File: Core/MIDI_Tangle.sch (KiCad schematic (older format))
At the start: 32 parts, among them J1 USB_C_Receptacle_USB2.0, J2 Conn_01x04, J4 Conn_01x06_Male, J5 Conn_01x08_Female, J6 Conn_01x08_Female, J7 Conn_01x08_Female, J8 Conn_01x08_Female, SW1 SW_Push_DPDT, U1 ATSAMD21G15B-A, U14 MCP2517FD-xSL, U15 TLE9250V, Y1 20MHz

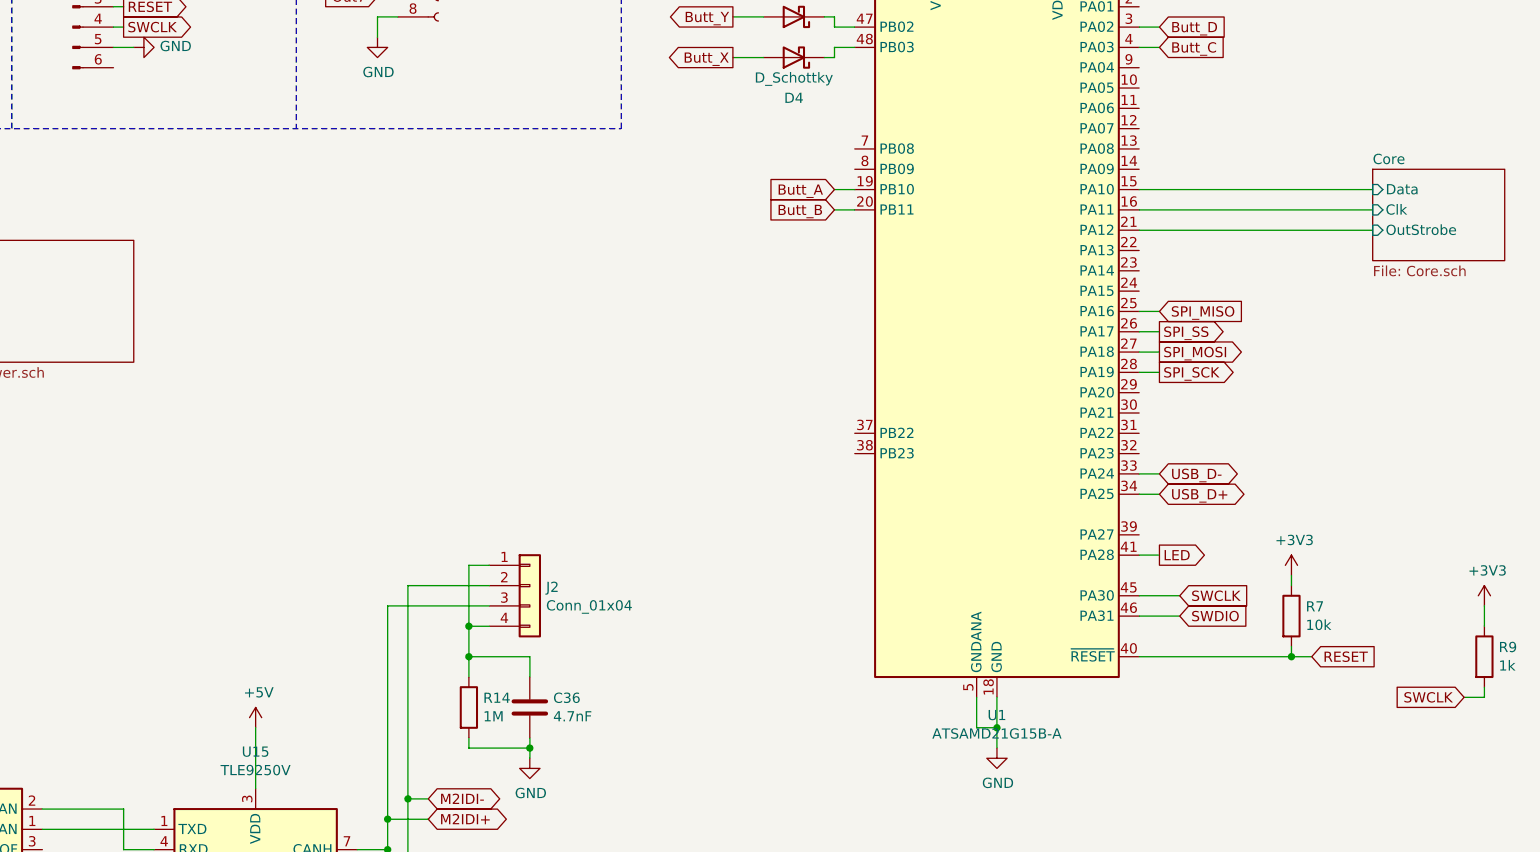
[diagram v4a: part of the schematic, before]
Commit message: Add bootloader buttons
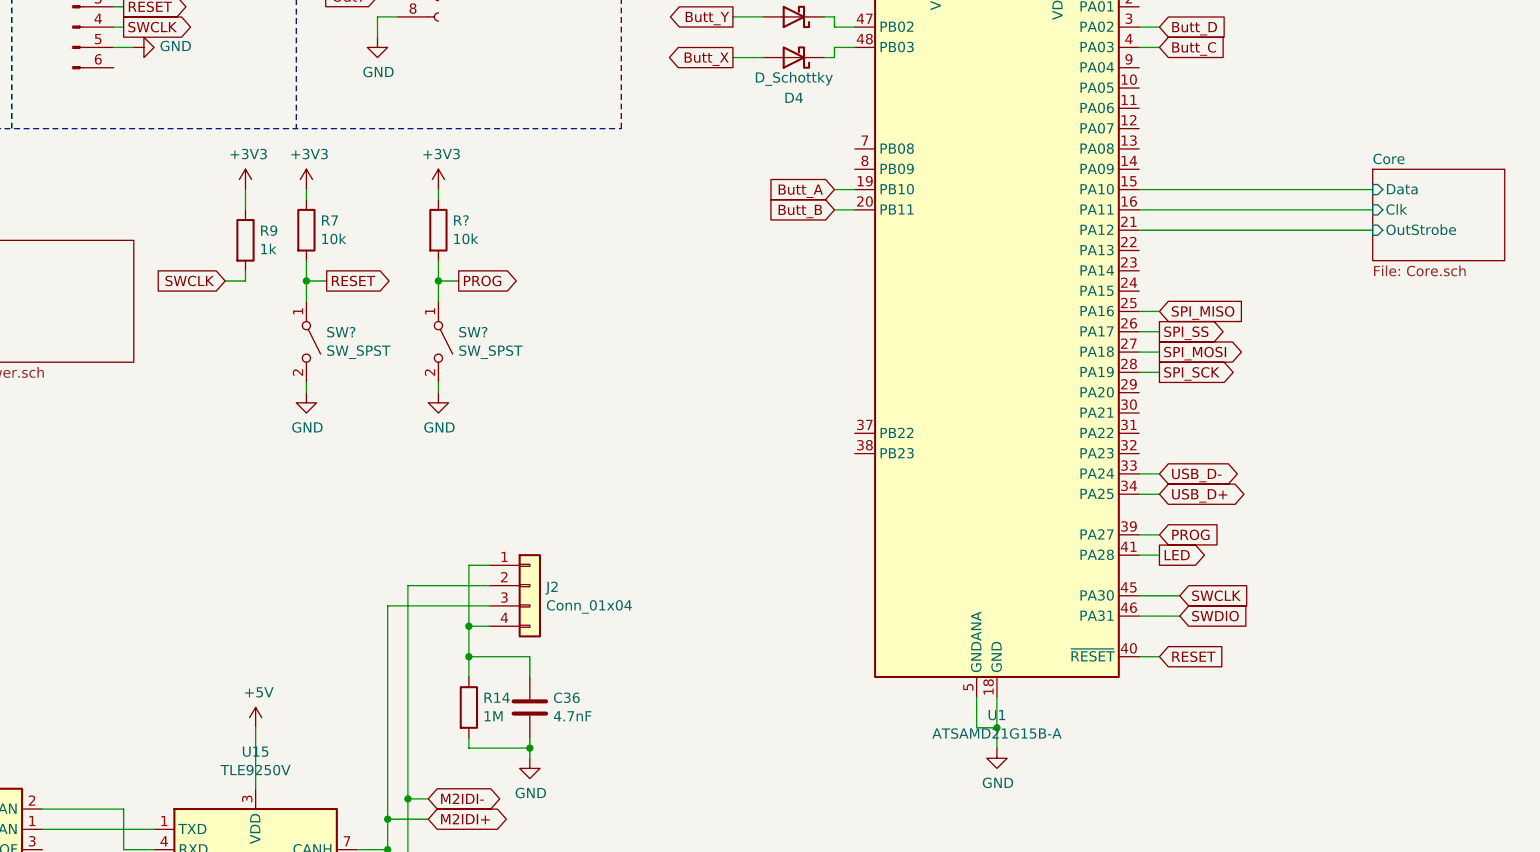
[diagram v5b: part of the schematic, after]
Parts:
- added R?: 10k, Resistor_SMD:R_0603_1608Metric, symbol Device:R
- added SW? (x2): SW_SPST, Custom_FP:Tactile_angled_5x5.4_SMD, symbol Switch:SW_SPST
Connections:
- net +3V3: now also R?.1
- net GND: now also SW?.2 (B), SW?.2 (B)
- net RESET: now also SW?.1 (A)
- net PROG: now reaches U1.39 (PA27)
- net PROG: now also R?.2, SW?.1 (A)
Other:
- moved on the sheet: R7, R9
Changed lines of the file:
@@
 Wire Wire Line
 	8450 5500 8650 5500
-Text GLabel 9300 5800 2    50   Input ~ 0
+Text GLabel 8550 5800 2    50   Input ~ 0
 RESET
 $Comp
@@
 LED
 Wire Wire Line
-	9300 5800 9200 5800
+	8550 5800 8450 5800
 $Comp
 L Device:C C3
@@
 L Device:R R7
 U 1 1 60DE3924
-P 9200 5600
-F 0 "R7" H 9270 5646 50  0000 L CNN
-F 1 "10k" H 9270 5555 50  0000 L CNN
-F 2 "Resistor_SMD:R_0603_1608Metric" V 9130 5600 50  0001 C CNN
-F 3 "~" H 9200 5600 50  0001 C CNN
-	1    9200 5600
-	1    0    0    -1
-$EndComp
-Wire Wire Line
-	9200 5750 9200 5800
-Wire Wire Line
-	9200 5800 8450 5800
+P 4350 3700
+F 0 "R7" H 4420 3746 50  0000 L CNN
+F 1 "10k" H 4420 3655 50  0000 L CNN
+F 2 "Resistor_SMD:R_0603_1608Metric" V 4280 3700 50  0001 C CNN
+F 3 "~" H 4350 3700 50  0001 C CNN
+	1    4350 3700
+	1    0    0    -1
+$EndComp
 $Comp
 L power:+3V3 #PWR0110
 U 1 1 60DF374E
-P 9200 5400
-F 0 "#PWR0110" H 9200 5250 50  0001 C CNN
-F 1 "+3V3" H 9215 5573 50  0000 C CNN
-F 2 "" H 9200 5400 50  0001 C CNN
-F 3 "" H 9200 5400 50  0001 C CNN
-	1    9200 5400
-	1    0    0    -1
-$EndComp
-Wire Wire Line
-	9200 5400 9200 5450
+P 4350 3500
+F 0 "#PWR0110" H 4350 3350 50  0001 C CNN
+F 1 "+3V3" H 4365 3673 50  0000 C CNN
+F 2 "" H 4350 3500 50  0001 C CNN
+F 3 "" H 4350 3500 50  0001 C CNN
+	1    4350 3500
+	1    0    0    -1
+$EndComp
+Wire Wire Line
+	4350 3500 4350 3550
 $Comp
 L Device:R R2
@@
 L Device:R R9
 U 1 1 60ED0663
-P 10150 5800
-F 0 "R9" H 10220 5846 50  0000 L CNN
-F 1 "1k" H 10220 5755 50  0000 L CNN
-F 2 "Resistor_SMD:R_0603_1608Metric" V 10080 5800 50  0001 C CNN
-F 3 "~" H 10150 5800 50  0001 C CNN
-	1    10150 5800
+P 4050 3750
+F 0 "R9" H 4120 3796 50  0000 L CNN
+F 1 "1k" H 4120 3705 50  0000 L CNN
+F 2 "Resistor_SMD:R_0603_1608Metric" V 3980 3750 50  0001 C CNN
+F 3 "~" H 4050 3750 50  0001 C CNN
+	1    4050 3750
 	1    0    0    -1
 $EndComp
@@
 L power:+3V3 #PWR0175
 U 1 1 60ED1510
-P 10150 5550
-F 0 "#PWR0175" H 10150 5400 50  0001 C CNN
-F 1 "+3V3" H 10165 5723 50  0000 C CNN
-F 2 "" H 10150 5550 50  0001 C CNN
-F 3 "" H 10150 5550 50  0001 C CNN
-	1    10150 5550
-	1    0    0    -1
-$EndComp
-Text GLabel 10050 6000 0    50   Input ~ 0
+P 4050 3500
+F 0 "#PWR0175" H 4050 3350 50  0001 C CNN
+F 1 "+3V3" H 4065 3673 50  0000 C CNN
+F 2 "" H 4050 3500 50  0001 C CNN
+F 3 "" H 4050 3500 50  0001 C CNN
+	1    4050 3500
+	1    0    0    -1
+$EndComp
+Text GLabel 3950 3950 0    50   Input ~ 0
 SWCLK
 Wire Wire Line
-	10050 6000 10150 6000
-Wire Wire Line
-	10150 6000 10150 5950
-Wire Wire Line
-	10150 5650 10150 5550
+	3950 3950 4050 3950
+Wire Wire Line
+	4050 3950 4050 3900
+Wire Wire Line
+	4050 3600 4050 3500
 Wire Wire Line
 	6150 1200 6250 1200
@@
 	0    1    1    0
 $EndComp
-Connection ~ 9200 5800
 $Sheet
 S 9600 3400 650  450
@@
 Wire Wire Line
 	8450 3700 9600 3700
+Text GLabel 4450 3950 2    50   Output ~ 0
+RESET
+Wire Wire Line
+	4450 3950 4350 3950
+Connection ~ 4350 3950
+Wire Wire Line
+	4350 3950 4350 4050
+Wire Wire Line
+	4350 3850 4350 3950
+$Comp
+L Switch:SW_SPST SW?
+U 1 1 65133670
+P 4350 4250
+F 0 "SW?" V 4304 4348 50  0000 L CNN
+F 1 "SW_SPST" V 4395 4348 50  0000 L CNN
+F 2 "Custom_FP:Tactile_angled_5x5.4_SMD" H 4350 4250 50  0001 C CNN
+F 3 "~" H 4350 4250 50  0001 C CNN
+	1    4350 4250
+	0    1    1    0
+$EndComp
+$Comp
+L power:GND #PWR?
+U 1 1 65133EF2
+P 4350 4500
+F 0 "#PWR?" H 4350 4250 50  0001 C CNN
+F 1 "GND" H 4355 4327 50  0000 C CNN
+F 2 "" H 4350 4500 50  0001 C CNN
+F 3 "" H 4350 4500 50  0001 C CNN
+	1    4350 4500
+	1    0    0    -1
+$EndComp
+Wire Wire Line
+	4350 4500 4350 4450
+$Comp
+L Device:R R?
+U 1 1 65140F2B
+P 5000 3700
+F 0 "R?" H 5070 3746 50  0000 L CNN
+F 1 "10k" H 5070 3655 50  0000 L CNN
+F 2 "Resistor_SMD:R_0603_1608Metric" V 4930 3700 50  0001 C CNN
+F 3 "~" H 5000 3700 50  0001 C CNN
+	1    5000 3700
+	1    0    0    -1
+$EndComp
+$Comp
+L power:+3V3 #PWR?
+U 1 1 65140F31
+P 5000 3500
+F 0 "#PWR?" H 5000 3350 50  0001 C CNN
+F 1 "+3V3" H 5015 3673 50  0000 C CNN
+F 2 "" H 5000 3500 50  0001 C CNN
+F 3 "" H 5000 3500 50  0001 C CNN
+	1    5000 3500
+	1    0    0    -1
+$EndComp
+Wire Wire Line
+	5000 3500 5000 3550
+Text GLabel 5100 3950 2    50   Output ~ 0
+PROG
+Wire Wire Line
+	5100 3950 5000 3950
+Connection ~ 5000 3950
+Wire Wire Line
+	5000 3950 5000 4050
+Wire Wire Line
+	5000 3850 5000 3950
+$Comp
+L Switch:SW_SPST SW?
+U 1 1 65140F3D
+P 5000 4250
+F 0 "SW?" V 4954 4348 50  0000 L CNN
+F 1 "SW_SPST" V 5045 4348 50  0000 L CNN
+F 2 "Custom_FP:Tactile_angled_5x5.4_SMD" H 5000 4250 50  0001 C CNN
+F 3 "~" H 5000 4250 50  0001 C CNN
+	1    5000 4250
+	0    1    1    0
+$EndComp
+$Comp
+L power:GND #PWR?
+U 1 1 65140F43
+P 5000 4500
+F 0 "#PWR?" H 5000 4250 50  0001 C CNN
+F 1 "GND" H 5005 4327 50  0000 C CNN
+F 2 "" H 5000 4500 50  0001 C CNN
+F 3 "" H 5000 4500 50  0001 C CNN
+	1    5000 4500
+	1    0    0    -1
+$EndComp
+Wire Wire Line
+	5000 4500 5000 4450
+Text GLabel 8550 5200 2    50   Input ~ 0
+PROG
+Wire Wire Line
+	8550 5200 8450 5200
 $EndSCHEMATC

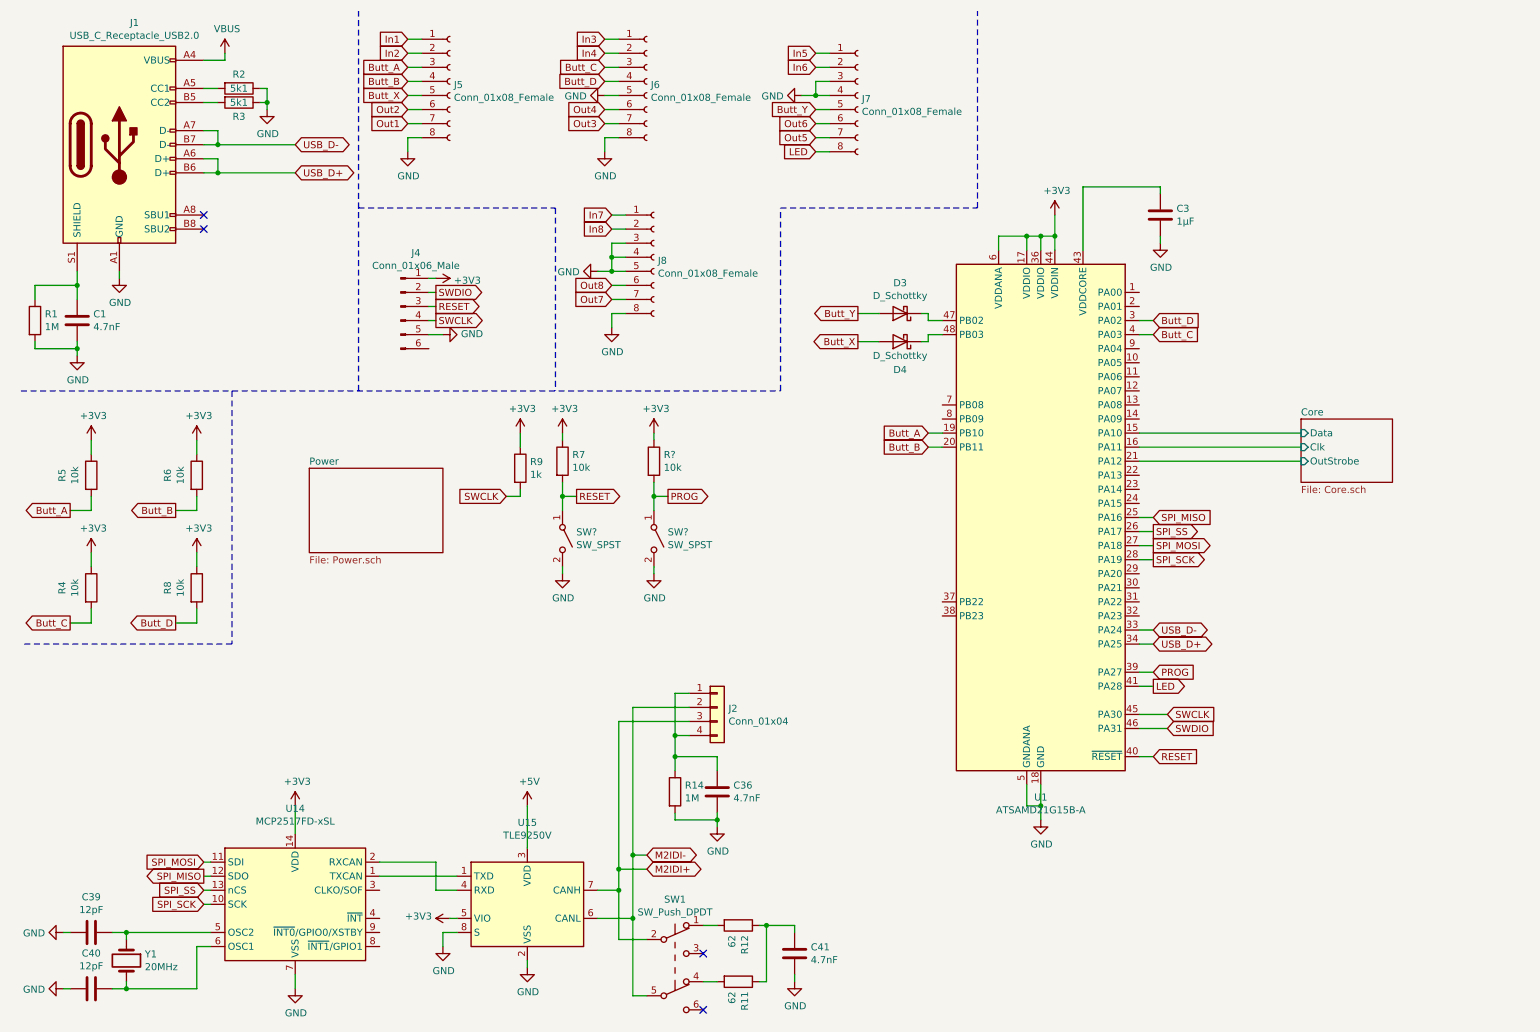
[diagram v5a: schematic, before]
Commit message: Add EEPROM
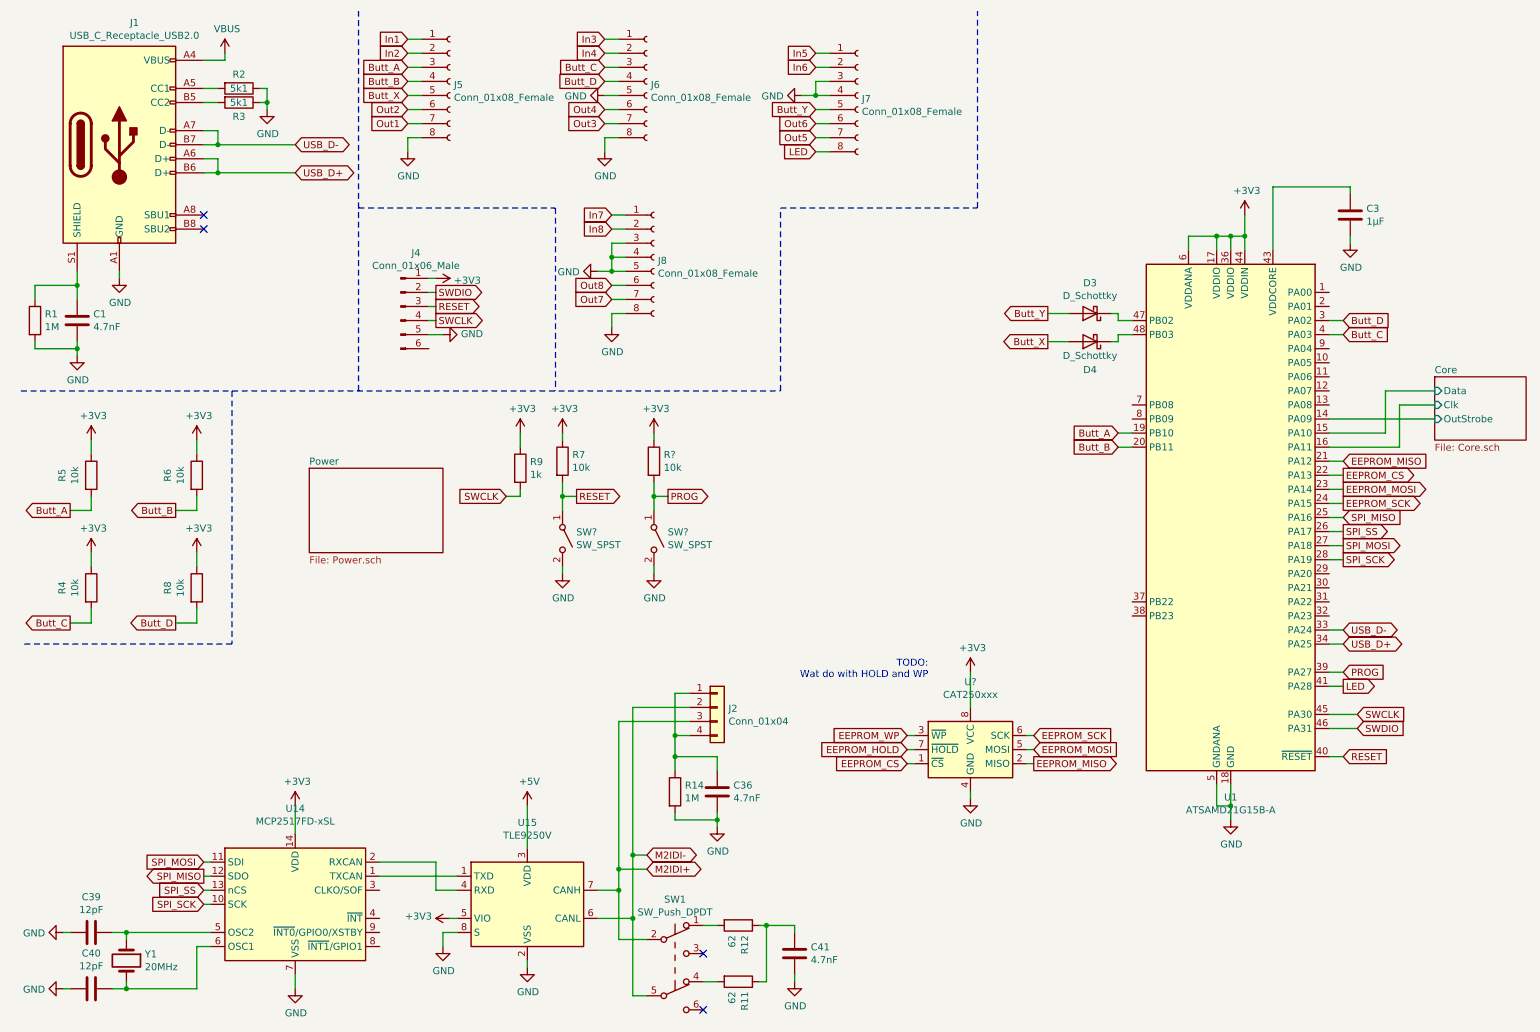
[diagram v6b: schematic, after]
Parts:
- added U?: CAT250xxx, symbol Memory_EEPROM:CAT250xxx
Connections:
- net +3V3: now also U?.8 (VCC)
- net Core/OutStrobe: now also U1.14 (PA09); no longer U1.21 (PA12)
- net GND: now also U?.4 (GND)
- net EEPROM_CS: now reaches U1.22 (PA13)
- net EEPROM_CS: now also U?.1 (~CS)
- net EEPROM_MOSI: now reaches U1.23 (PA14)
- net EEPROM_MOSI: now also U?.5 (MOSI)
- net EEPROM_SCK: now reaches U1.24 (PA15)
- net EEPROM_SCK: now also U?.6 (SCK)
- new net EEPROM_HOLD: U?.7 (~HOLD)
- new net EEPROM_MISO: U1.21 (PA12), U?.2 (MISO)
- new net EEPROM_WP: U?.3 (~WP)
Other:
- note added: "TODO:\nWat do with HOLD and WP"
- moved on the sheet: C3, D3, D4, U1
